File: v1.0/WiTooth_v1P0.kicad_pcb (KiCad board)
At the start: 4 copper layers, 67 x 25.8 mm, 65 parts, among them P1 USB_A_MALE, P4 CONN_01X20, P5 CONN_01X20, Q1 Q_NPN_EBC, Q2 Q_NPN_EBC, SW1 RESET, SW2 BOOT, SW3 USER_SW, U1 AMS1117-3V3, U2 CP2102, U3 ESP-32_WROOM32_Rectangle, Y1 Crystal

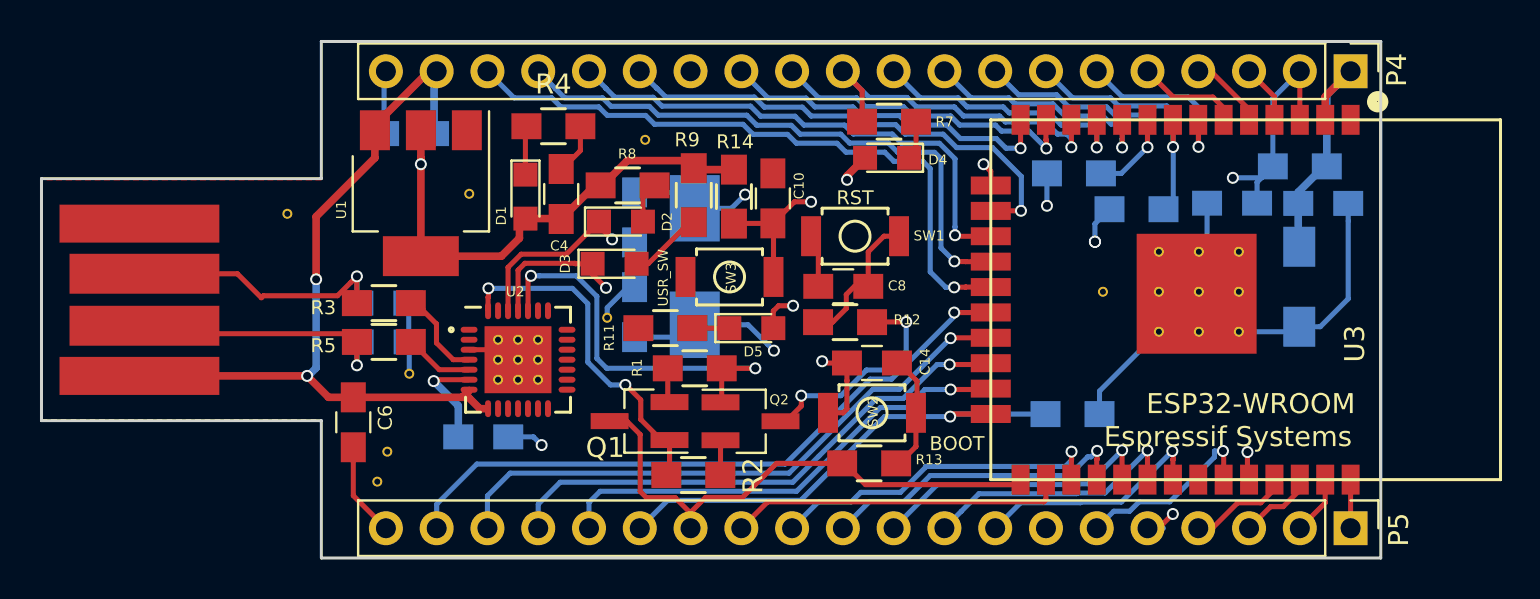
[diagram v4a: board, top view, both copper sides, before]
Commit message: BOM generated and Routing Done
- Bom generated
- Routing Completed
- Silk Screen Added
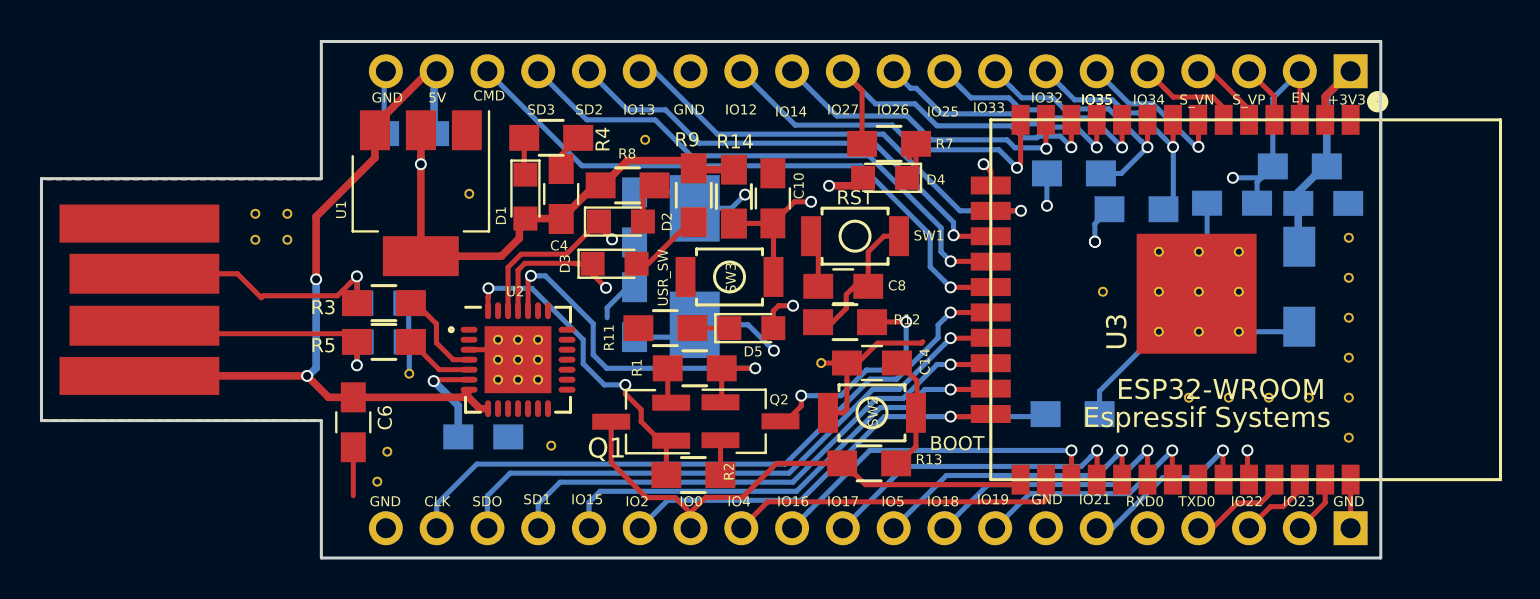
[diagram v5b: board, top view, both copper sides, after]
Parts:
- removed the REF** at (126.3, 100.9)
- added REF**: VIA_0.5mm, via:VIA_0.5mm, F.Cu at (110.3, 97.0)
- added REF**: VIA_0.5mm, via:VIA_0.5mm, F.Cu at (163.4, 106.9)
- added REF**: VIA_0.5mm, via:VIA_0.5mm, F.Cu at (163.4, 104.9)
- added REF**: VIA_0.5mm, via:VIA_0.5mm, F.Cu at (163.4, 102.9)
- added REF**: VIA_0.5mm, via:VIA_0.5mm, F.Cu at (163.4, 100.9)
- added REF**: VIA_0.5mm, via:VIA_0.5mm, F.Cu at (163.4, 98.9)
- added REF**: VIA_0.5mm, via:VIA_0.5mm, F.Cu at (163.4, 96.9)
- added REF**: VIA_0.5mm, via:VIA_0.5mm, F.Cu at (108.7, 97.0)
- added REF**: VIA_0.5mm, via:VIA_0.5mm, F.Cu at (108.7, 95.7)
- added REF**: Fab Details table, Fab Details table:Fab Details table, F.Cu at (57.7, 86.6)
- added REF**: VIA_0.5mm, via:VIA_0.5mm, F.Cu at (137.0, 103.2)
- added REF**: VIA_0.5mm, via:VIA_0.5mm, F.Cu at (123.5, 107.3)
- added REF**: VIA_0.5mm, via:VIA_0.5mm, F.Cu at (155.4, 104.9)
- added REF**: VIA_0.5mm, via:VIA_0.5mm, F.Cu at (157.4, 104.9)
- added REF**: VIA_0.5mm, via:VIA_0.5mm, F.Cu at (159.4, 104.9)
- added REF**: VIA_0.5mm, via:VIA_0.5mm, F.Cu at (161.4, 104.9)
- P4, P5: moved to B.Cu
- Q1, Q2: value Q_NPN_EBC -> 2N3904-MMBT
- R8, R9: value R -> 1K
- moved R7 1.11 mm to (140.4, 92.2)
- moved D4 1.00 mm to (140.2, 93.9)
- moved R4 0.59 mm to (123.5, 91.9)
- moved Q1 0.09 mm to (128.0, 106.1)
- turned P4 to 90 degrees
- turned P5 to 90 degrees
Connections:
- U2 pad 1: (no net) -> Net-(U2-Pad1)
- U2 pad 10: (no net) -> Net-(U2-Pad10)
- U2 pad 11: (no net) -> Net-(U2-Pad11)
- U2 pad 12: (no net) -> Net-(U2-Pad12)
- U2 pad 13: (no net) -> Net-(U2-Pad13)
- U2 pad 14: (no net) -> Net-(U2-Pad14)
- U2 pad 15: (no net) -> Net-(U2-Pad15)
- U2 pad 16: (no net) -> Net-(U2-Pad16)
- U2 pad 17: (no net) -> Net-(U2-Pad17)
- U2 pad 18: (no net) -> Net-(U2-Pad18)
- U2 pad 19: (no net) -> Net-(U2-Pad19)
- U2 pad 2: (no net) -> Net-(U2-Pad2)
- U2 pad 20: (no net) -> Net-(U2-Pad20)
- U2 pad 21: (no net) -> Net-(U2-Pad21)
- U2 pad 22: (no net) -> Net-(U2-Pad22)
- U2 pad 23: (no net) -> Net-(U2-Pad23)
- U2 pad 27: (no net) -> Net-(U2-Pad27)
- U2 pad 9: (no net) -> Net-(U2-Pad9)
- U3 pad 32: (no net) -> Net-(U3-Pad32)
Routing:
- net GND: track 58.4 -> 50.0 mm, vias 3 -> 1
- net RXD0: track 56.1 -> 52.9 mm, vias 3 -> 2
- net CMD: track 32.7 -> 30.6 mm
- net SD3: track 29.2 -> 27.3 mm
- net SD2: track 25.8 -> 23.9 mm
- net IO12: track 17.0 -> 18.3 mm
- net DTR: track 18.0 -> 16.8 mm
- net IO35: track 31.6 -> 30.5 mm
- net IO13: track 24.5 -> 23.5 mm
- net IO32: track 13.6 -> 12.6 mm
- net IO27: track 17.5 -> 18.5 mm
- net RTS: track 20.2 -> 19.3 mm
- net IO33: track 14.2 -> 13.4 mm
- net IO26: track 13.7 -> 13.1 mm
- net Net-(D1-Pad1): track 2.44 -> 1.86 mm
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- added copper zone on B.Cu, net GND
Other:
- board text added: "+3V3"
- board text added: "5V"
- board text added: "CLK"
- board text added: "CMD"
- board text added: "EN"
- board text added: "GND"
- board text added: "IO0"
- board text added: "IO12"
- board text added: "IO13"
- board text added: "IO14"
- board text added: "IO15"
- board text added: "IO16"
- board text added: "IO17"
- board text added: "IO18"
- board text added: "IO19"
- board text added: "IO2"
- board text added: "IO21"
- board text added: "IO22"
- board text added: "IO23"
- board text added: "IO25"
- board text added: "IO26"
- board text added: "IO27"
- board text added: "IO32"
- board text added: "IO33"
- board text added: "IO34"
- board text added: "IO35"
- board text added: "IO4"
- board text added: "IO5"
- board text added: "RXD0"
- board text added: "SD1"
- board text added: "SD2"
- board text added: "SD3"
- board text added: "SDO"
- board text added: "S_VN"
- board text added: "S_VP"
- board text added: "TXD0"
- board text added: "thingtronics.com"
